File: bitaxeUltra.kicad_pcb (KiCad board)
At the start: 4 copper layers, 56.5 x 99.8 mm, 147 parts, among them J4 Conn_01x04, J5 TC2030-IDC, J6 Conn_01x06, J8 USB_C_Receptacle_USB2.0, J9 Conn_01x04, Q1 DMP31D1U-7, SW1 GT-TC029B-H025-L1N, SW2 GT-TC029B-H025-L1N, U1 25MHz, U10 DS4432U+, U11 AP63203QWU-7, U12 ESP32-S3-WROOM-1, U13 AP7375-50SA-7, U14 BM1366_mode1, U15 74LVC1G08, U2 TXB0104RGYR, U4 CH224K, U5 MCP1824T-1202E/OT, U6 MCP1824T-0802E, U7 EMC2101, U8 INA260, U9 SIC431AED-T1-GE3, Y1 32.768kHz

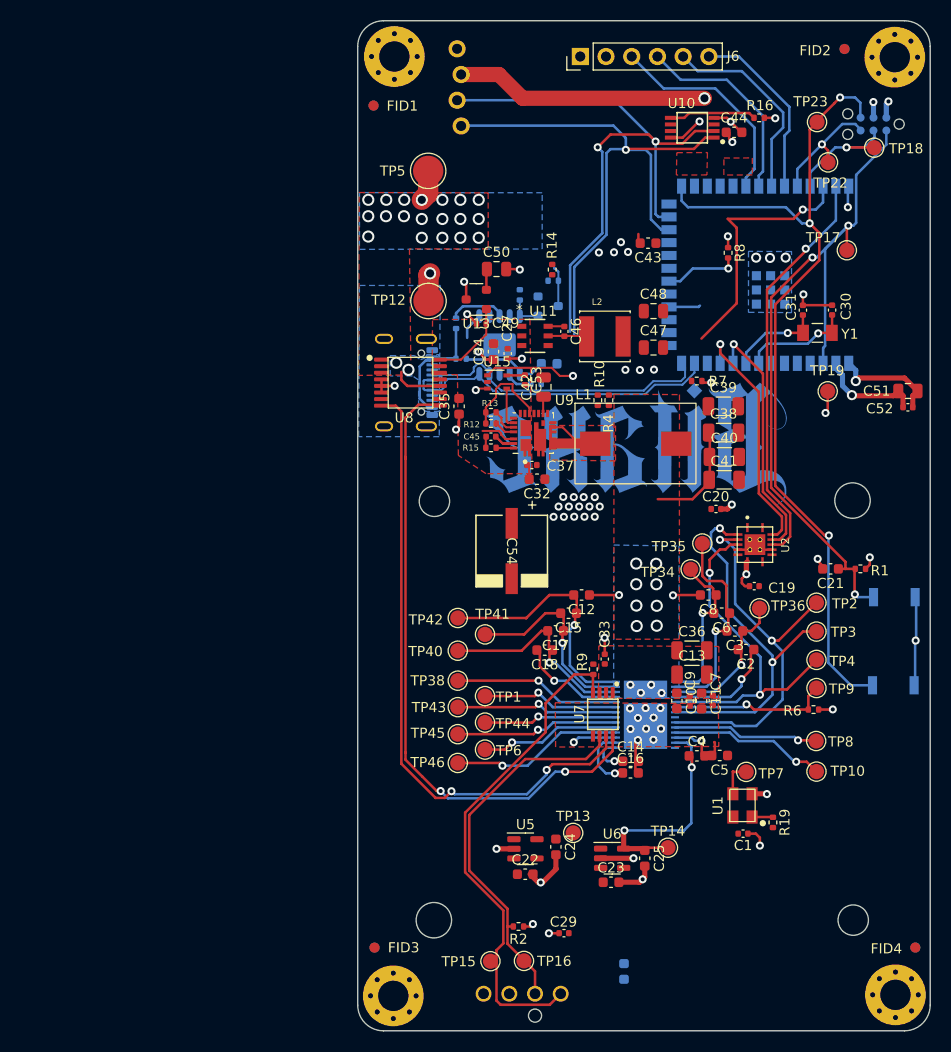
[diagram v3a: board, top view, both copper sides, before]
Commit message: 3.3V net fix, PCB progress
Fixed accidental use of both 3V3 and 3.3V to just use 3V3. Worked on PCB
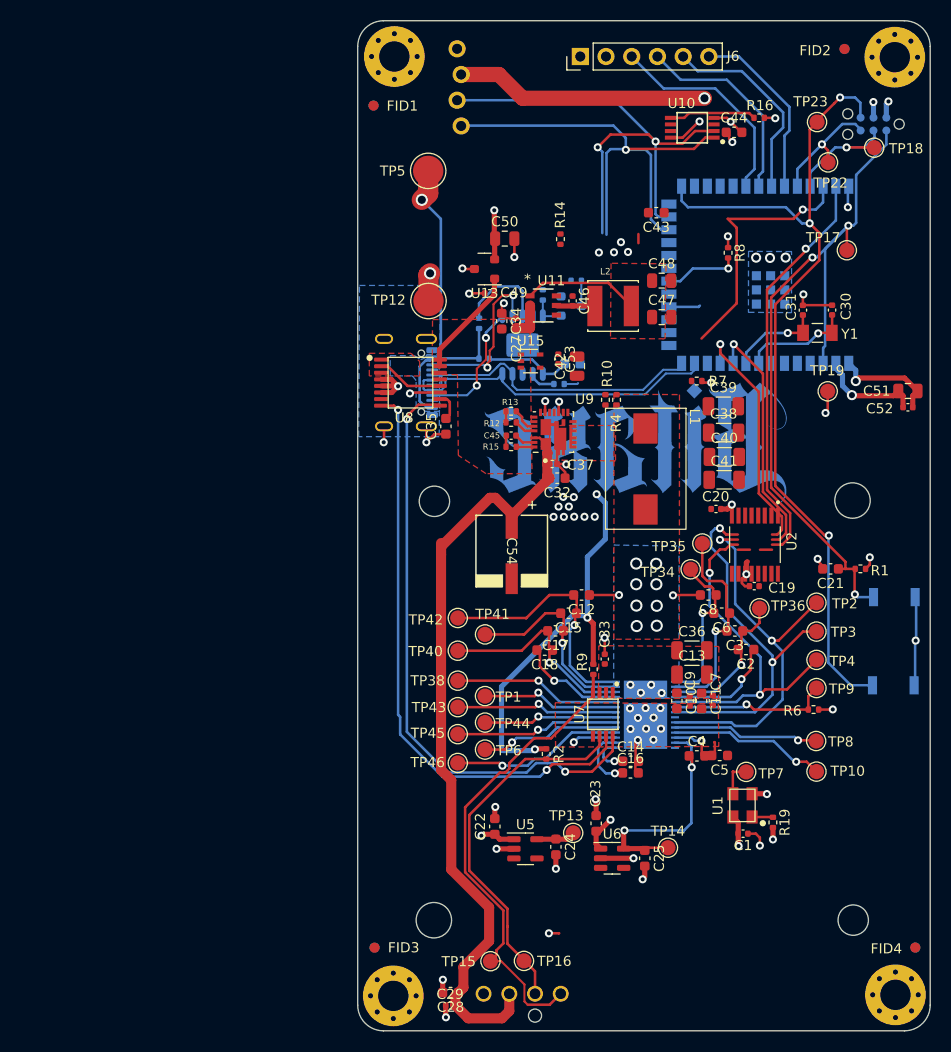
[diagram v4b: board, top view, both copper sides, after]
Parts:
- C28: moved to F.Cu
- U2: value TXB0104RGYR -> SN74AVC4T774PWR; footprint bitaxe:TXB0104 -> bitaxe:SOP65P640X120-16N
- moved R2 17.3 mm to (95.8, 119.9), turned to 90 degrees
- moved C28 17.3 mm to (86.4, 143.5), turned to 180 degrees
- moved C29 13.3 mm to (86.4, 144.8)
- moved C23 6.00 mm to (100.7, 126.8), turned to 90 degrees
- moved C22 5.59 mm to (90.7, 127.1), turned to 90 degrees
- moved C42 3.90 mm to (98.9, 81.6)
- moved C53 3.90 mm to (97.0, 80.9)
- moved U15 3.90 mm to (94.3, 81.1)
- moved C34 3.12 mm to (91.4, 77.2), turned to -90 degrees
- moved C46 3.12 mm to (98.4, 75.2)
- moved L2 3.12 mm to (102.4, 75.7)
- moved C27 3.12 mm to (92.8, 77.4), turned to 90 degrees
- moved C48 3.12 mm to (107.2, 73.2)
- moved C49 3.12 mm to (90.2, 74.4)
- moved C43 3.12 mm to (106.7, 66.5)
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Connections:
- C1 pad 2: +3.3V -> +3V3
- C20 pad 1: +3.3V -> +3V3
- R19 pad 2: +3.3V -> +3V3
- R2 pad 2: +3V3 -> +5V
- U1 pad 4: +3.3V -> +3V3
- U2 pad 1: +1V8 -> GND
- U2 pad 11: /RST -> /BM1366/RO
- U2 pad 12: /TX -> /BM1366/CLKI_HI
- U2 pad 13: /RX -> /RST
- U2 pad 14: +3.3V -> /TX
- U2 pad 15: GND -> +3V3
- U2 pad 16: GND -> +1V2
- U2 pad 2: /BM1366/RO -> GND
- U2 pad 5: GND -> /BM1366/CLKI
- U2 pad 6: unconnected-(U2-NC-Pad6) -> /RX
- U2 pad 8: +1V8 -> +1V2
- U2 pad 9: unconnected-(U2-NC-Pad9) -> GND
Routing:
- net +12V: track 13.1 -> 92.8 mm
- net +5V: track 2.07 -> 45.2 mm, vias 0 -> 4
- net +3V3: track 49.3 -> 72.4 mm, vias 9 -> 12
- net IN+: track 19.6 -> 40.9 mm, vias 21 -> 1
- net GND: track 112.9 -> 129.7 mm, vias 66 -> 65
- net Net-(J8-CC2): track 0.00 -> 16.5 mm, vias 0 -> 2
- net /SDA: track 122.5 -> 107.2 mm
- net /SCL: track 125.5 -> 111.3 mm
- net /VDD: track 42.5 -> 31.2 mm
- net Net-(Q1-D): track 13.3 -> 2.50 mm, vias 1 -> 0
- net Net-(J8-CC1): track 2.64 -> 12.7 mm, vias 0 -> 2
- net Net-(L1-Pad1): track 8.78 -> 0.00 mm
- net /Power/VOUT_INTERNAL: track 9.28 -> 1.10 mm
- net /Power/ASIC_EN: track 3.99 -> 0.00 mm
- net +1V2: track 0.00 -> 3.84 mm
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- added copper zone on In2.Cu, net +5V

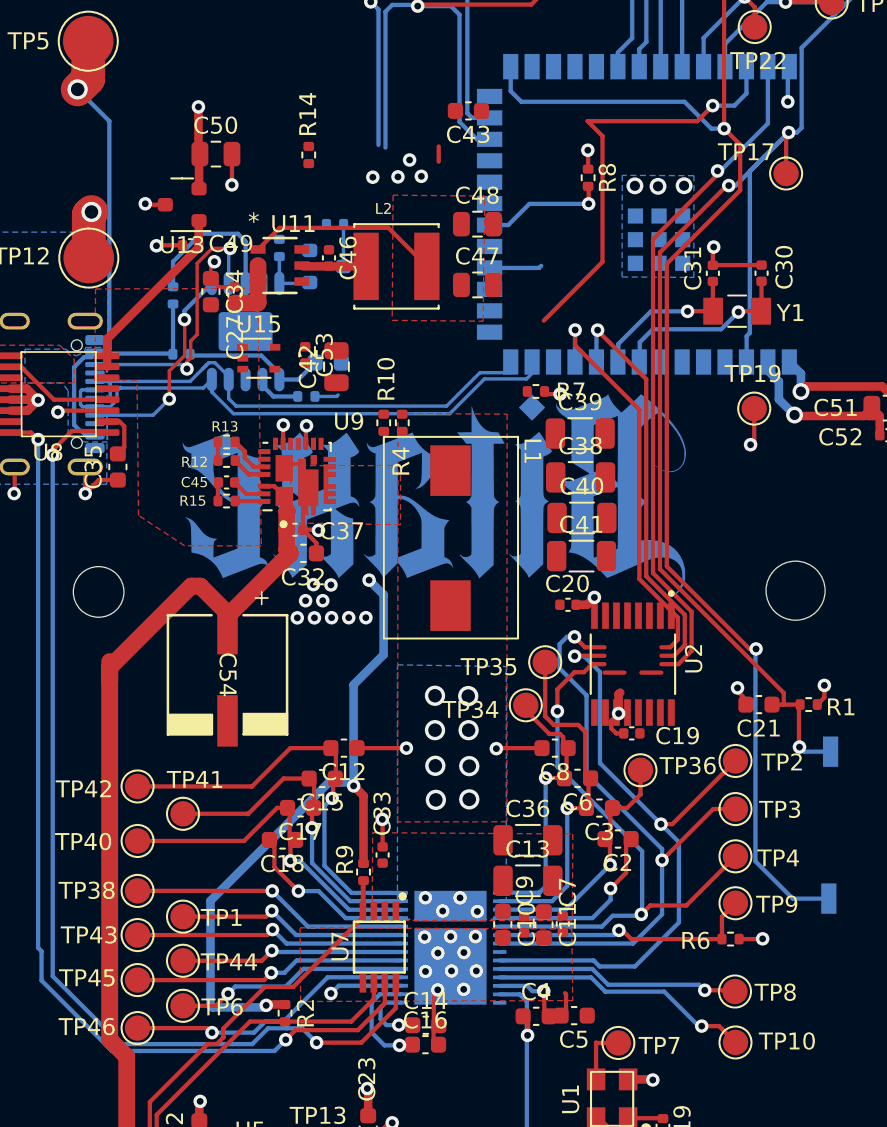
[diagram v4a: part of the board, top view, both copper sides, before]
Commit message: Layout work
Working on power supplies - moved VDD south, added nice planes for it. Started cleaning up around new level shifter.
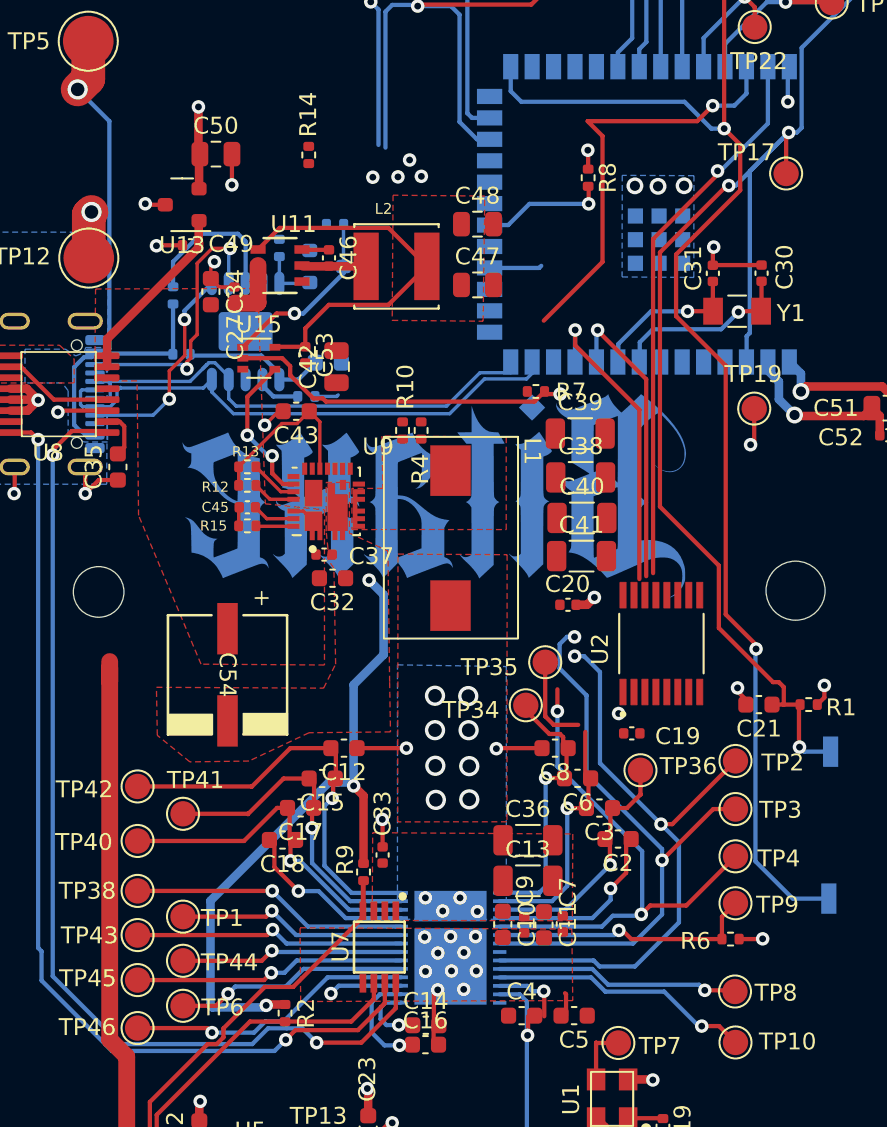
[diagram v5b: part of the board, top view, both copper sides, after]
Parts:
- moved C43 20.5 mm to (96.5, 84.3)
- moved C37 2.27 mm to (98.1, 92.8)
- moved U9 2.27 mm to (98.2, 89.6)
- moved C32 2.27 mm to (98.6, 94.2)
- moved U2 2.08 mm to (118.1, 98.0), turned to 90 degrees
- moved C45 1.92 mm to (93.6, 90.0)
- moved R12 1.92 mm to (93.6, 88.7)
- moved R13 1.92 mm to (93.6, 87.6)
- moved R15 1.92 mm to (93.6, 91.1)
- moved R10 1.21 mm to (102.8, 85.4)
- moved R4 1.21 mm to (103.9, 85.4)
- moved C4 0.86 mm to (109.8, 120.1)
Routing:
- net /ESP32/PWR_EN: track 4.10 -> 23.6 mm
- net +12V: track 92.8 -> 73.6 mm
- net GND: track 129.7 -> 116.0 mm, vias 65 -> 54
- net +3V3: track 72.4 -> 84.0 mm
- net /Power/VOUT_INTERNAL: track 1.10 -> 10.3 mm
- net /Power/ASIC_EN: track 0.00 -> 9.13 mm, vias 0 -> 2
- net Net-(Q1-D): track 2.50 -> 10.7 mm, vias 0 -> 1
- net /RST: track 40.6 -> 32.9 mm
- net /TX: track 24.4 -> 17.7 mm
- net /RX: track 23.9 -> 18.2 mm
- net /BM1366/RST_N: track 34.5 -> 31.1 mm
- net /BM1366/RO: track 37.6 -> 35.5 mm
- net /BM1366/CI: track 38.3 -> 36.5 mm
- net Net-(U11-BST): track 0.00 -> 1.61 mm
- net /ESP32/IO0: track 85.7 -> 85.0 mm
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
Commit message: Layout completed for concept 1
Need to still work on vias and fills, move some parts around.
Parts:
- moved R19 41.8 mm to (119.8, 84.9), turned to 180 degrees
- moved C1 37.4 mm to (120.2, 90.7), turned to 0 degrees
- moved U1 36.9 mm to (119.6, 88.3), turned to 180 degrees
- moved R14 16.7 mm to (110.3, 79.5), turned to 180 degrees
- moved C44 9.20 mm to (105.2, 58.4), turned to 90 degrees
- moved R7 7.57 mm to (103.3, 81.5), turned to -90 degrees
- moved R10 6.59 mm to (96.2, 86.1), turned to 180 degrees
- moved C19 3.36 mm to (114.2, 100.8)
- moved C42 2.72 mm to (101.0, 83.3)
- moved C43 2.66 mm to (98.7, 85.8), turned to 0 degrees
- moved C47 2.29 mm to (106.6, 79.0), turned to -90 degrees
- moved C48 1.94 mm to (106.7, 71.3), turned to 90 degrees
- moved R4 0.67 mm to (104.4, 85.0), turned to 180 degrees
- moved C16 0.42 mm to (104.3, 122.2)
- moved R17 0.36 mm to (97.2, 83.1)
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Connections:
- U2 pad 1: GND -> +1V2
- U2 pad 11: /BM1366/RO -> /BM1366/CLKI_HI
- U2 pad 12: /BM1366/CLKI_HI -> /RST
- U2 pad 13: /RST -> /TX
- U2 pad 14: /TX -> /RX
- U2 pad 3: /BM1366/CI -> /BM1366/RO
- U2 pad 4: /BM1366/RST_N -> /BM1366/CI
- U2 pad 5: /BM1366/CLKI -> /BM1366/RST_N
- U2 pad 6: /RX -> /BM1366/CLKI
- U2 pad 8: +1V2 -> GND
- U9 pad 11: unconnected-(U9-GL-Pad10) -> unconnected-(U9-GL-Pad11)
- U9 pad 28: unconnected-(U9-GL-Pad10) -> unconnected-(U9-GL-Pad28)
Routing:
- net +1V2: track 3.84 -> 95.5 mm, vias 0 -> 4
- net /Power/ASIC_EN: track 9.13 -> 81.3 mm, vias 2 -> 6
- net GND: track 116.0 -> 165.9 mm, vias 54 -> 68
- net /Power/VDD_FB: track 0.00 -> 47.2 mm, vias 0 -> 4
- net +3V3: track 84.0 -> 124.7 mm, vias 12 -> 25
- net /BM1366/CLKI: track 3.51 -> 31.5 mm, vias 0 -> 2
- net /VDD: track 31.2 -> 58.1 mm, vias 15 -> 17
- net /ESP32/PGOOD: track 0.00 -> 23.4 mm, vias 0 -> 1
- net /SCL: track 111.3 -> 133.9 mm
- net /SDA: track 107.2 -> 128.9 mm
- net +12V: track 73.6 -> 84.1 mm
- net /BM1366/RST_N: track 31.1 -> 40.3 mm
- net /BM1366/CLKI_HI: track 0.00 -> 6.17 mm
- net /BM1366/RO: track 35.5 -> 29.8 mm, vias 2 -> 1
- net Net-(U9-VDRV): track 0.00 -> 4.87 mm
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
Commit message: Release Candidate 205pd
Everything ordered. Let's see how it goes!
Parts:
- moved R19 42.1 mm to (129.3, 126.0)
- moved U1 41.4 mm to (127.8, 128.9)
- moved C1 41.4 mm to (128.4, 131.3)
- moved U2 31.0 mm to (120.6, 129.0), turned to 0 degrees
- moved C20 30.2 mm to (123.2, 124.1), turned to 90 degrees
- moved C19 25.8 mm to (121.6, 125.5)
- moved C35 18.6 mm to (89.2, 69.2), turned to -90 degrees
- moved U8 14.8 mm to (83.3, 68.4)
- moved U13 11.0 mm to (92.4, 61.4), turned to 90 degrees
- moved C49 10.3 mm to (91.0, 64.2)
- moved C50 6.61 mm to (95.6, 63.7), turned to -90 degrees
- moved C51 2.69 mm to (128.9, 84.5)
- moved C52 2.69 mm to (128.9, 86.1)
- moved C37 0.45 mm to (98.0, 93.2)
- moved C32 0.36 mm to (98.6, 94.5)
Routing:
- net /TX: track 19.1 -> 59.1 mm
- net /RST: track 34.9 -> 74.9 mm
- net /RX: track 19.3 -> 58.7 mm
- net +1V2: track 95.5 -> 65.4 mm, vias 4 -> 1
- net IN+: track 40.9 -> 19.2 mm, vias 4 -> 8
- net GND: track 165.9 -> 154.2 mm, vias 68 -> 80
- net +12V: track 84.1 -> 72.8 mm
- net /BM1366/CI: track 32.9 -> 43.7 mm, vias 1 -> 2
- net /BM1366/RO: track 29.8 -> 40.1 mm
- net /BM1366/CLKI: track 31.5 -> 22.8 mm, vias 2 -> 1
- net /BM1366/RST_N: track 40.3 -> 33.5 mm, vias 2 -> 1
- net /SCL: track 133.9 -> 128.6 mm, vias 4 -> 3
- net /BM1366/CLKI_HI: track 6.17 -> 3.26 mm
- net +5V: track 45.2 -> 42.7 mm, vias 4 -> 11
- net /SDA: track 128.9 -> 127.4 mm
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- added copper zone on F.Cu, net +5V
